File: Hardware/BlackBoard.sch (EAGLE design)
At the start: 68 parts, among them IC3 LM1117, J1 microB, J2 ICSP, J3 POWER_JACKSUPER_BOMB_DIGITY, Q1 1A/60V/500mΩ, Q2 2N7002PW, Q3 2N7002PW, U2 CH340G, U3 AP2112-3.3V, U4 ATMEGA328P_TQFP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

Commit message: Readme update. Schematic compression.
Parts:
- removed FRAME1: FRAME-LEDGER, SparkFun-Aesthetics:FRAME-LEDGER
- added FRAME2: FRAME-LETTER, SparkFun-Aesthetics:FRAME-LETTER
- D1: value MBRA140 -> SS14TR
- J1: value microB -> AMP FCI 10103594-0001LF; device SparkFun-Connectors:USB_MICRO-B_HALF_PTH -> SparkFun-Connectors:USB_MICRO-B_HALF_PTH_MILL
- J2: value ICSP -> ISP
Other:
- note added: "Qwiic 3.3V Conversion"
- note added: "X01"
- note removed: "3.3V Regulation"
- note removed: "v23"
- moved on the sheet: C1, C10, C11, C12, C15, C16, C17, C18, C2, C3, C4, C5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

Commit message: Cleanup for release of v2
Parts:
- removed C11, C7: 22pF, SparkFun-Capacitors:22PF-0603-50V-5%
- removed J1: AMP FCI 10103594-0001LF, SparkFun-Connectors:USB_MICRO-B_HALF_PTH_MILL
- removed LED5: GREEN, SparkFun-LED:LED-GREEN_HIDDENSILK
- removed U2: CH340G, SparkFun-DigitalIC:CH340GSMD
- removed Y2: 12MHz, USB Basic:CRYSTAL-GROUNDED3.2X2.5
- added D2: GREEN, SparkFun-LED:LED-GREENLILYPAD
- added J5: USB C, USB-C:USB_C16PIN
- added JP14: USB_SOLDER_PADS, SparkFun-Connectors:USB_SOLDER_PADS
- added QW1, QW2: JUMPER-SMT_2_NC_TRACE_SILK, SparkFun-Jumpers:JUMPER-SMT_2_NC_TRACE_SILK
- added R7, R8: 5.1k, SparkFun-Resistors:5.1KOHM5.1KOHM-0603-1/10W-1%
- added U5: CH340C, SparkFun-IC-Comms:CH340C
- C16: device SparkFun-Capacitors:1.0UF-16V-10%(0603) -> SparkFun-Capacitors:1.0UF-0603-16V-10%
- C17: device SparkFun-Capacitors:10NF/10000PF-50V-10%(0603) -> SparkFun-Capacitors:10NF-0603-50V-10%
- C18: device SparkFun-Capacitors:0.1UF-25V(+80/-20%)(0603) -> SparkFun-Capacitors:0.1UF-0603-25V-(+80/-20%)
- D1: value SS14TR -> 1A/40V/500mV; device SparkFun-DiscreteSemi:MBRA140 -> SparkFun-DiscreteSemi:DIODE-SCHOTTKY-SS14
- F1: value PPTC_6V500MA -> 6V 0.5A
- J2: PROD_ID CONN-11415 -> (none)
- LED2: device SparkFun-LED:LED-GREEN_HIDDENSILK -> SparkFun-LED:LED-GREENLILYPAD; PROD_ID DIO-09910 -> (none)
- Q1: value 1A/60V/500mΩ -> 1.1A/60V/600mΩ; device SparkFun-DiscreteSemi:MOSFET-PCH-ZXMP6A13F -> SparkFun-DiscreteSemi:MOSFET_PCH-SI2309DS
- Q2, Q3: value 2N7002PW -> 310mA/60V/1.6Ω
- S1: value RESET -> Tall Switch; device SparkFun-Electromechanical:SWITCH_SPST_4_PINSQUARE -> SparkFun-Switches:MOMENTARY-SWITCH-SPST-SMD-5.2-TALL-REDUNDANT
- renumbered FRAME2 to FRAME1
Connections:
- removed net N$11: C11.2, U2.XO, Y2.2
- removed net N$12: C7.2, U2.XI, Y2.1
- removed net N$13: J1.D-, U2.UD-
- removed net N$14: J1.D+, U2.UD+
- removed net V3: C17.1, U2.V3
- new net CC1: J5.CC1, R8.2
- new net CC2: J5.CC2, R7.2
- new net D+: J5.D+, JP14.3, U5.UD+
- new net D-: J5.D-, JP14.2, U5.UD-
- new net N$45: Q3.D, QW2.2, R6.1
- new net N$6: C17.1, U5.V3
- new net N$7: Q2.D, QW1.2, R13.1
- net !DTR: now also U5.!DTR; no longer U2.!DTR
- net AD4/SDA: now also QW2.1; no longer Q3.D, R6.1
- net AD5/SCL: now also QW1.1; no longer Q2.D, R13.1
- net GND: now also J5.GND, JP14.4, R7.1, R8.1, U4.GND, U5.GND; no longer C11.1, C7.1, J1.GND, S1.2, U2.GND, U4.GND@3, U4.GND@5, Y2.GND
- net N$5: now also D2.A; no longer LED5.A
- net RESET: now also S1.2; no longer S1.3, S1.4
- net RX-I: now also U5.TXO; no longer U2.TXD
- net SHLD: now also J5.SHLD; no longer J1.SHIELD
- net TX-O: now also D2.C, U5.RXI; no longer LED5.C, U2.RXD
- net VCC: now also U4.VCC, U5.VCC; no longer U2.VCC, U4.VCC@4, U4.VCC@6
- net VUSB: now also J5.VBUS, JP14.1; no longer J1.VBUS
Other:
- note added: "Note: Cut QW1 and QW2 to disconnect Qwiic and allow A4/A5 as analog inputs."
- note added: "X02"
- note removed: "X01"
- moved on the sheet: C1, C10, C12, C15, C17, C18, C2, C8, D3, F1, J2, J4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

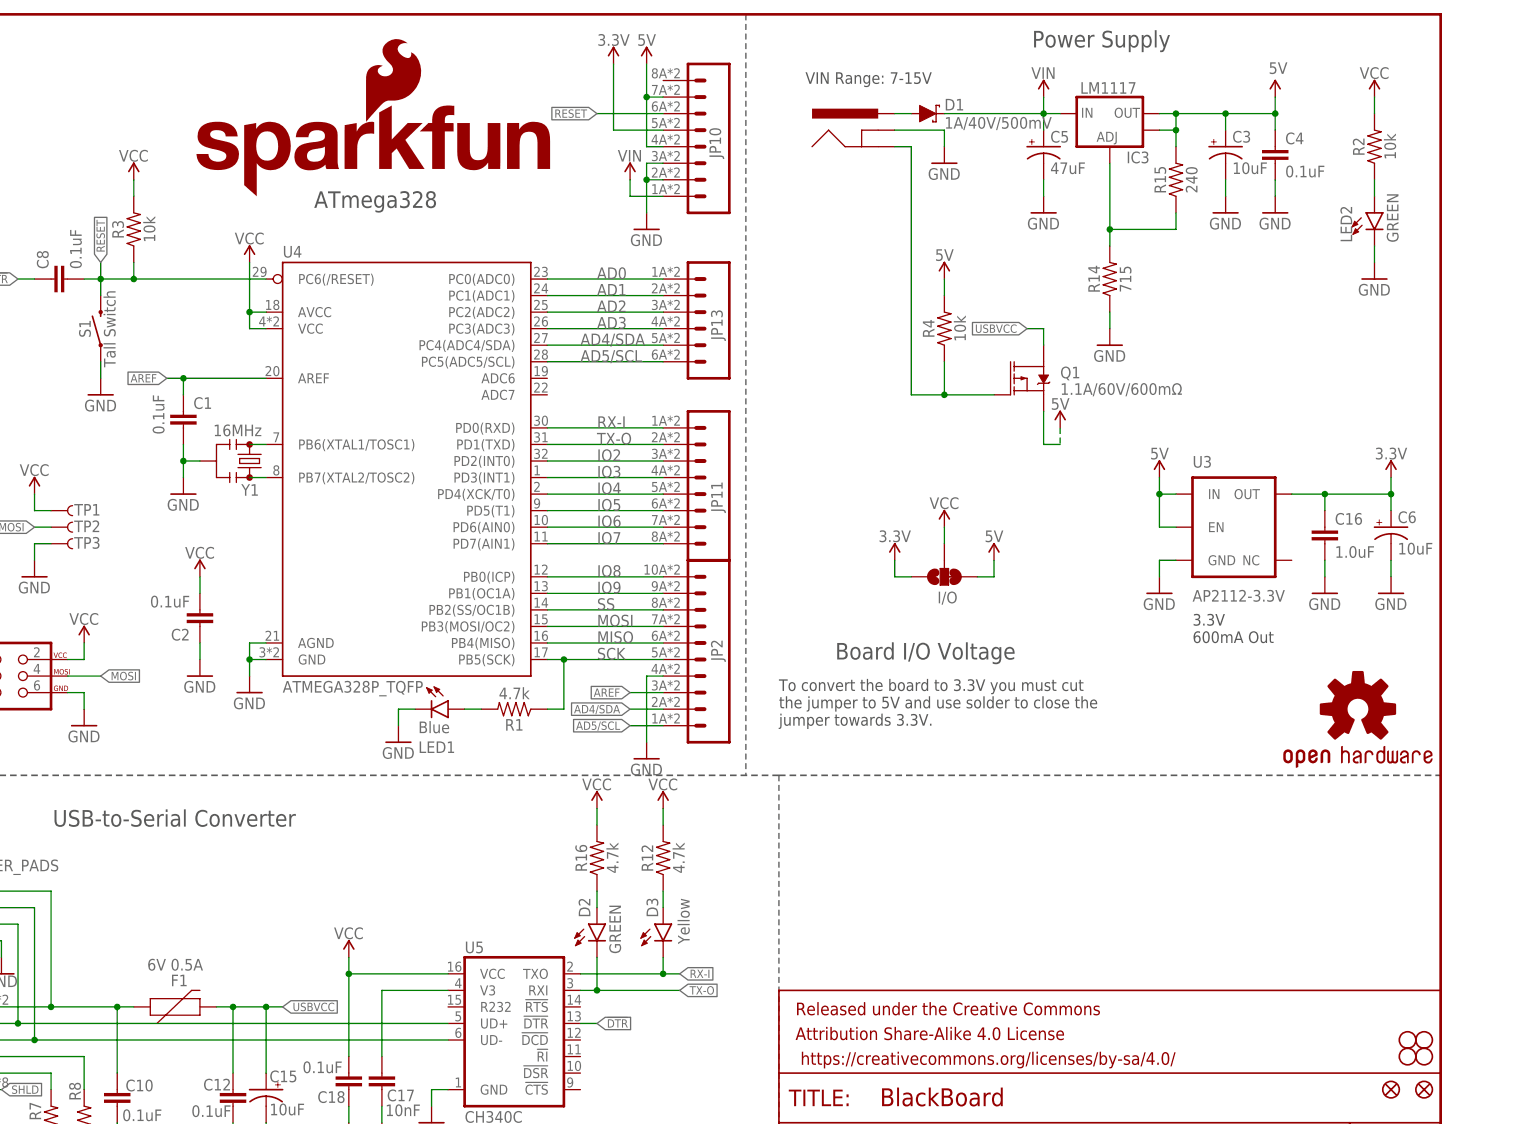
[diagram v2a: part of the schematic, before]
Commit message: Swap to larger PTC. Correct connection to IOREF.
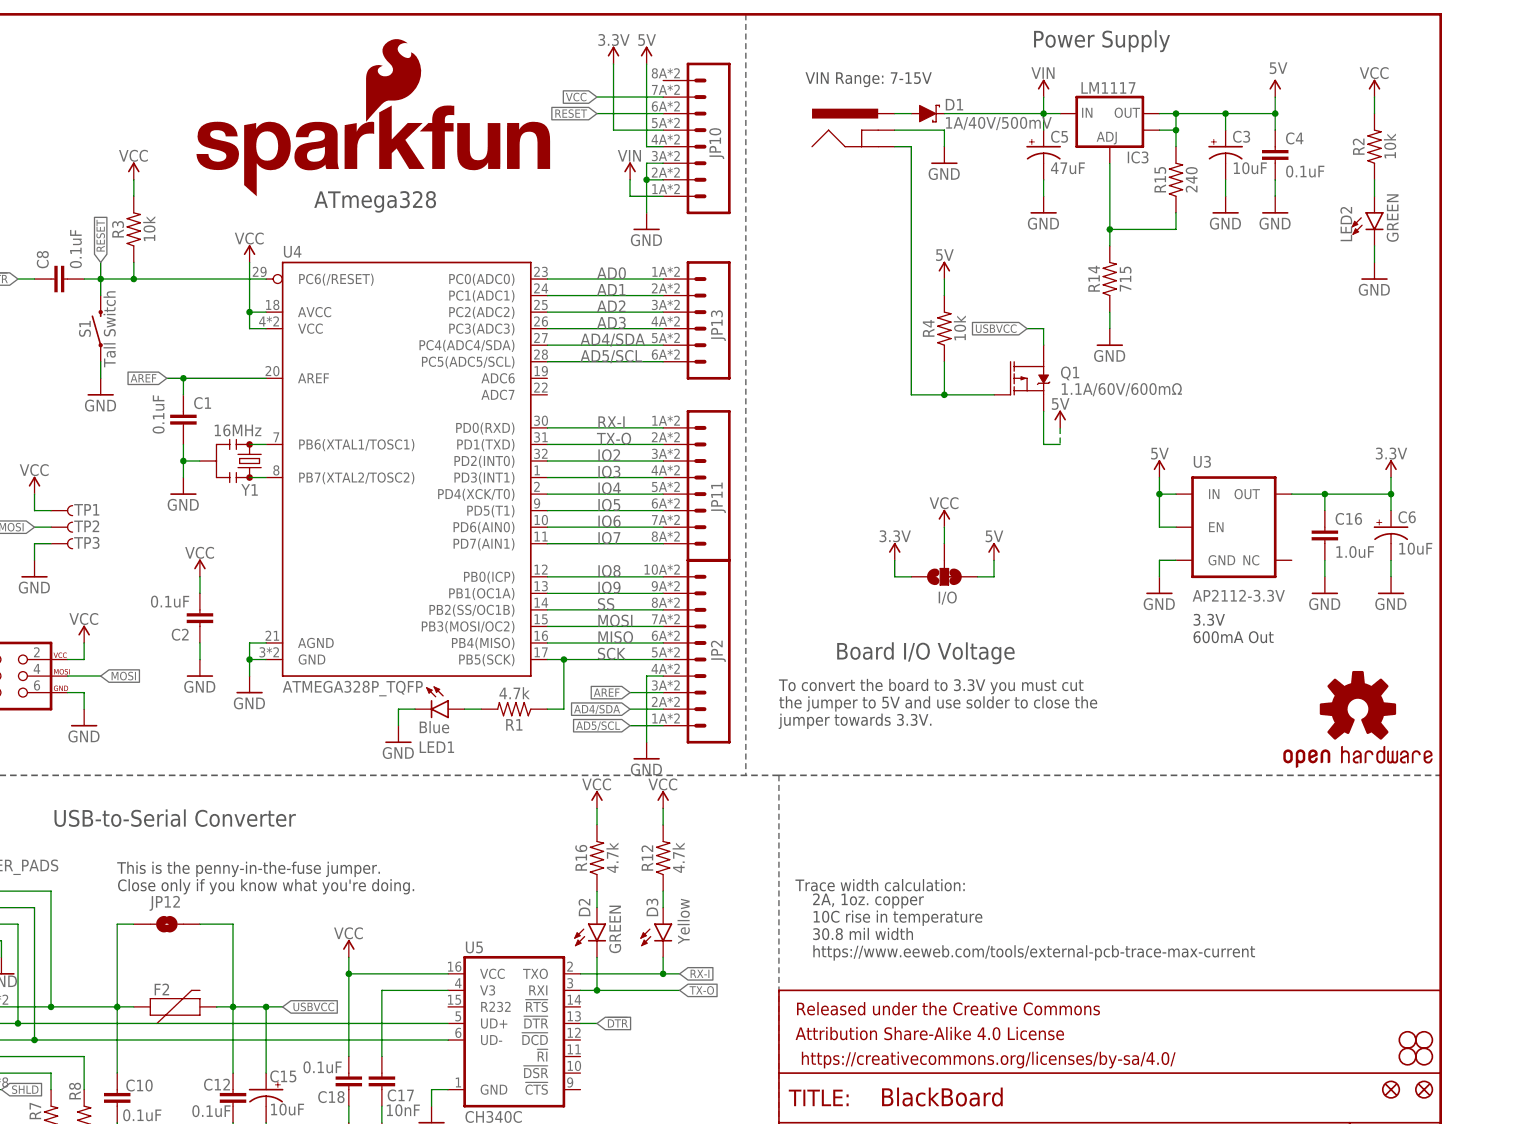
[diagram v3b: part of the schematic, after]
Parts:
- removed F1: 6V 0.5A, SparkFun-Fuses:PPTC_6V500MA
- added F2: 6V_2A, SparkFun-Fuses:PPTC_2A
- added JP12: JUMPER-SMT_2_NO_SILK, SparkFun-Jumpers:JUMPER-SMT_2_NO_SILK
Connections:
- net 5V: no longer JP10.7
- net USBVCC: now also F2.2, JP12.2; no longer F1.2
- net VCC: now also JP10.7
- net VUSB: now also F2.1, JP12.1; no longer F1.1
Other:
- note added: "2A, 1oz. copper 10C rise in temperature 30.8 mil width https://www.eeweb.com/tools/external-pcb-trace-max-current"
- note added: "This is the penny-in-the-fuse jumper. Close only if you know what you're doing."
- note added: "Trace width calculation:"
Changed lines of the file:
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@@
 <?xml version="1.0" encoding="utf-8"?>
 <!DOCTYPE eagle SYSTEM "eagle.dtd">
-<eagle version="9.2.1">
+<eagle version="9.3.0">
 <drawing>
 <settings>
@@
 <class number="0" name="default" width="0" drill="0">
 </class>
-<class number="1" name="power" width="0.1778" drill="0">
+<class number="1" name="power" width="0.762" drill="0">
 </class>
 </classes>
@@
 <part name="SUPPLY7" library="SparkFun-PowerSymbols" deviceset="VIN" device=""/>
 <part name="D1" library="SparkFun-DiscreteSemi" deviceset="DIODE-SCHOTTKY" device="-SS14" value="1A/40V/500mV"/>
-<part name="F1" library="SparkFun-Fuses" deviceset="PPTC" device="_6V500MA" value="6V 0.5A"/>
 <part name="JP11" library="SparkFun-Connectors" deviceset="M08" device="SMD-COMBO" value="JP11">
 <attribute name="PROD_ID" value="CONN-10204"/>
@@
 <part name="JP14" library="SparkFun-Connectors" deviceset="USB_SOLDER_PADS" device=""/>
 <part name="GND17" library="SparkFun-PowerSymbols" deviceset="GND" device=""/>
+<part name="JP12" library="SparkFun-Jumpers" deviceset="JUMPER-SMT_2_NO" device="_SILK" value=""/>
+<part name="F2" library="SparkFun-Fuses" deviceset="PPTC" device="_2A" value="6V_2A"/>
 </parts>
 <sheets>
@@
 <text x="271.78" y="20.32" size="2.54" layer="97">Note: Cut QW1 and QW2 to disconnect
 Qwiic and allow A4/A5 as analog inputs.</text>
+<text x="45.72" y="50.8" size="1.778" layer="97" font="vector">This is the penny-in-the-fuse jumper.
+Close only if you know what you're doing.</text>
+<text x="149.86" y="50.8" size="1.778" layer="97" font="vector">Trace width calculation:</text>
+<text x="152.4" y="40.64" size="1.778" layer="97" font="vector">2A, 1oz. copper
+10C rise in temperature
+30.8 mil width
+https://www.eeweb.com/tools/external-pcb-trace-max-current</text>
 </plain>
 <instances>
@@
 <attribute name="VALUE" x="172.72" y="167.8686" size="1.778" layer="96"/>
 </instance>
-<instance part="F1" gate="F1" x="53.34" y="33.02" smashed="yes">
-<attribute name="NAME" x="55.245" y="36.195" size="1.778" layer="95" font="vector" align="bottom-center"/>
-<attribute name="VALUE" x="54.61" y="40.386" size="1.778" layer="96" font="vector" align="top-center"/>
-</instance>
 <instance part="JP11" gate="G$1" x="134.62" y="114.3" smashed="yes" rot="R180">
 <attribute name="VALUE" x="138.684" y="108.966" size="1.778" layer="96" font="vector" rot="R90"/>
@@
 <instance part="GND17" gate="1" x="27.94" y="38.1" smashed="yes">
 <attribute name="VALUE" x="27.94" y="37.846" size="1.778" layer="96" align="top-center"/>
+</instance>
+<instance part="JP12" gate="G$1" x="53.34" y="45.72" smashed="yes">
+<attribute name="NAME" x="50.8" y="48.26" size="1.778" layer="95" font="vector"/>
+<attribute name="VALUE" x="50.8" y="43.18" size="1.778" layer="96" font="vector" align="top-left"/>
+</instance>
+<instance part="F2" gate="F1" x="53.34" y="33.02" smashed="yes">
+<attribute name="NAME" x="52.578" y="34.798" size="1.778" layer="95" font="vector" align="bottom-center"/>
 </instance>
 </instances>
@@
 </segment>
 </net>
-<net name="5V" class="0">
+<net name="5V" class="1">
 <segment>
 <wire x1="172.72" y1="144.78" x2="172.72" y2="142.24" width="0.1524" layer="91"/>
@@
 </segment>
 <segment>
-<pinref part="JP10" gate="G$1" pin="7"/>
-<wire x1="129.54" y1="172.72" x2="127" y2="172.72" width="0.1524" layer="91"/>
 <pinref part="SUPPLY3" gate="G$1" pin="5V"/>
-<wire x1="127" y1="172.72" x2="127" y2="177.8" width="0.1524" layer="91"/>
-<junction x="127" y="172.72"/>
 <pinref part="JP10" gate="G$1" pin="4"/>
 <wire x1="127" y1="165.1" x2="129.54" y2="165.1" width="0.1524" layer="91"/>
-<wire x1="127" y1="165.1" x2="127" y2="172.72" width="0.1524" layer="91"/>
+<wire x1="127" y1="165.1" x2="127" y2="177.8" width="0.1524" layer="91"/>
 </segment>
 <segment>
@@
 </segment>
 </net>
-<net name="VIN" class="0">
+<net name="VIN" class="1">
 <segment>
 <wire x1="124.46" y1="157.48" x2="129.54" y2="157.48" width="0.1524" layer="91"/>
@@
 </segment>
 </net>
-<net name="PWRIN" class="0">
+<net name="PWRIN" class="1">
 <segment>
 <wire x1="165.1" y1="170.18" x2="167.64" y2="170.18" width="0.1524" layer="91"/>
@@
 </segment>
 </net>
-<net name="USBVCC" class="0">
+<net name="USBVCC" class="1">
 <segment>
 <wire x1="187.96" y1="134.62" x2="187.96" y2="137.16" width="0.1524" layer="91"/>
@@
 </segment>
 <segment>
-<pinref part="F1" gate="F1" pin="2"/>
 <pinref part="C15" gate="G$1" pin="+"/>
 <wire x1="60.96" y1="33.02" x2="63.5" y2="33.02" width="0.1524" layer="91"/>
@@
 <wire x1="68.58" y1="33.02" x2="71.12" y2="33.02" width="0.1524" layer="91"/>
 <junction x="68.58" y="33.02"/>
-</segment>
-</net>
-<net name="VUSB" class="0">
-<segment>
-<pinref part="F1" gate="F1" pin="1"/>
+<pinref part="JP12" gate="G$1" pin="2"/>
+<wire x1="58.42" y1="45.72" x2="63.5" y2="45.72" width="0.1524" layer="91"/>
+<wire x1="63.5" y1="45.72" x2="63.5" y2="33.02" width="0.1524" layer="91"/>
+<pinref part="F2" gate="F1" pin="2"/>
+</segment>
+</net>
+<net name="VUSB" class="1">
+<segment>
 <pinref part="C10" gate="G$1" pin="1"/>
 <wire x1="45.72" y1="33.02" x2="48.26" y2="33.02" width="0.1524" layer="91"/>
@@
 <wire x1="35.56" y1="50.8" x2="35.56" y2="33.02" width="0.1524" layer="91"/>
 <junction x="35.56" y="33.02"/>
+<pinref part="JP12" gate="G$1" pin="1"/>
+<wire x1="48.26" y1="45.72" x2="45.72" y2="45.72" width="0.1524" layer="91"/>
+<wire x1="45.72" y1="45.72" x2="45.72" y2="33.02" width="0.1524" layer="91"/>
+<pinref part="F2" gate="F1" pin="1"/>
 </segment>
 </net>
@@
 <pinref part="SUPPLY22" gate="G$1" pin="VCC"/>
 </segment>
-</net>
+<segment>
+<pinref part="JP10" gate="G$1" pin="7"/>
+<wire x1="129.54" y1="172.72" x2="119.38" y2="172.72" width="0.1524" layer="91"/>
+<label x="119.38" y="172.72" size="1.27" layer="95" rot="R180" xref="yes"/>
+</segment>
+</net>

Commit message: Adding panel
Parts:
- F2: value 6V_2A -> 6V/2A; device SparkFun-Fuses:PPTC_2A -> SparkFun-Fuses:PPTC_6V2A
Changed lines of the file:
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@@
 <part name="GND17" library="SparkFun-PowerSymbols" deviceset="GND" device=""/>
 <part name="JP12" library="SparkFun-Jumpers" deviceset="JUMPER-SMT_2_NO" device="_SILK" value=""/>
-<part name="F2" library="SparkFun-Fuses" deviceset="PPTC" device="_2A" value="6V_2A"/>
+<part name="F2" library="SparkFun-Fuses" deviceset="PPTC" device="_6V2A" value="6V/2A"/>
 </parts>
 <sheets>
@@
 </segment>
 </net>
-<net name="3.3V" class="0">
+<net name="3.3V" class="1">
 <segment>
 <wire x1="129.54" y1="167.64" x2="121.92" y2="167.64" width="0.1524" layer="91"/>

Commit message: Add switch for IO voltage. Add PTH holes.
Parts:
- removed I/O: JUMPER-SMT_3_1-NC_TRACE_SILK, SparkFun-Jumpers:JUMPER-SMT_3_1-NC_TRACE_SILK
- added BYP: JUMPER-SMT_2_NO_SILK, SparkFun-Jumpers:JUMPER-SMT_2_NO_SILK
- added JP15: (no value), SparkFun-Connectors:M08NO_SILK
- added JP18: (no value), SparkFun-Connectors:M06NO_SILK
- added JP19: (no value), SparkFun-Connectors:CONN_08NO_SILK_FEMALE_PTH
- added S2: (no value), SparkFun-Switches:SWITCH-DPDT-SMD-AYZ0202
- D3: value Yellow -> YELLOW
- FRAME1: value FRAME-LETTER -> FRAME-LEDGER; device SparkFun-Aesthetics:FRAME-LETTER -> SparkFun-Aesthetics:FRAME-LEDGER
- J4: value (none) -> QWIIC_RIGHT_ANGLE
- JP12: value JUMPER-SMT_2_NO_SILK -> M10NO_SILK; device SparkFun-Jumpers:JUMPER-SMT_2_NO_SILK -> SparkFun-Connectors:M10NO_SILK; PROD_ID (none) -> CONN-11219
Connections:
- removed net AD0: JP13.1, U4.PC0(ADC0)
- removed net AD1: JP13.2, U4.PC1(ADC1)
- removed net AD2: JP13.3, U4.PC2(ADC2)
- removed net AD3: JP13.4, U4.PC3(ADC3)
- removed net AD4/SDA: JP13.5, JP2.2, QW2.1, U4.PC4(ADC4/SDA)
- removed net AD5/SCL: JP13.6, JP2.1, QW1.1, U4.PC5(ADC5/SCL)
- removed net IO2: JP11.3, U4.PD2(INT0)
- removed net IO3: JP11.4, U4.PD3(INT1)
- removed net IO4: JP11.5, U4.PD4(XCK/T0)
- removed net IO5: JP11.6, U4.PD5(T1)
- removed net IO6: JP11.7, U4.PD6(AIN0)
- removed net IO7: JP11.8, U4.PD7(AIN1)
- removed net IO8: JP2.10, U4.PB0(ICP)
- removed net IO9: JP2.9, U4.PB1(OC1A)
- removed net RESET: C8.2, J2.5, JP10.6, R3.1, S1.2, TP6.1, U4.PC6(/RESET)
- removed net SS: JP2.8, U4.PB2(SS/OC1B)
- new net !RESET: C8.2, J2.5, JP10.6, JP15.6, R3.1, S1.2, TP6.1, U4.PC6(/RESET)
- new net A0: JP13.1, JP18.1, U4.PC0(ADC0)
- new net A1: JP13.2, JP18.2, U4.PC1(ADC1)
- new net A2: JP13.3, JP18.3, U4.PC2(ADC2)
- new net A3: JP13.4, JP18.4, U4.PC3(ADC3)
- new net A4/SDA: JP12.2, JP13.5, JP18.5, JP2.2, QW2.1, U4.PC4(ADC4/SDA)
- new net A5/SCL: JP12.1, JP13.6, JP18.6, JP2.1, QW1.1, U4.PC5(ADC5/SCL)
- new net D10: JP12.8, JP2.8, U4.PB2(SS/OC1B)
- new net D2: JP11.3, JP19.3, U4.PD2(INT0)
- new net D3: JP11.4, JP19.4, U4.PD3(INT1)
- new net D4: JP11.5, JP19.5, U4.PD4(XCK/T0)
- new net D5: JP11.6, JP19.6, U4.PD5(T1)
- new net D6: JP11.7, JP19.7, U4.PD6(AIN0)
- new net D7: JP11.8, JP19.8, U4.PD7(AIN1)
- new net D8: JP12.10, JP2.10, U4.PB0(ICP)
- new net D9: JP12.9, JP2.9, U4.PB1(OC1A)
- net 3.3V: now also JP15.5, S2.1, S2.4; no longer I/O.1
- net 5V: now also JP15.4, S2.3, S2.6; no longer I/O.3
- net AREF: now also JP12.3
- net GND: now also JP12.4, JP15.2, JP15.3
- net MISO: now also JP12.6
- net MOSI: now also JP12.7
- net RX-I: now also JP19.1
- net SCK: now also JP12.5
- net TX-O: now also JP19.2
- net USBVCC: now also BYP.2; no longer JP12.2
- net VCC: now also JP15.7, S2.2, S2.5; no longer I/O.2
- net VIN: now also JP15.1
- net VUSB: now also BYP.1; no longer JP12.1
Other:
- note added: "PTH Connections"
- note added: "SMD Headers"
- note added: "Slide the switch to change the I/O Voltage. Applying tape over switch is recommended to prevent accidental change."
- note added: "This switch is limited to 1.2VA."
- note added: "X04"
- note removed: "To convert the board to 3.3V you must cut the jumper to 5V and use solder to close the jumper towards 3.3V."
- note removed: "X02"
- moved on the sheet: C1, C16, C2, C3, C4, C5, C6, C8, D1, IC3, J2, J4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
